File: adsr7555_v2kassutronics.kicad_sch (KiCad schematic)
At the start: 43 parts, among them J1 Power, J2 GateIn, J5 InvOut, J6 Output, Q1 3904, Q2 3904, Q3 3904, SW1 SW_Trig, U1 7555, U2 TL074

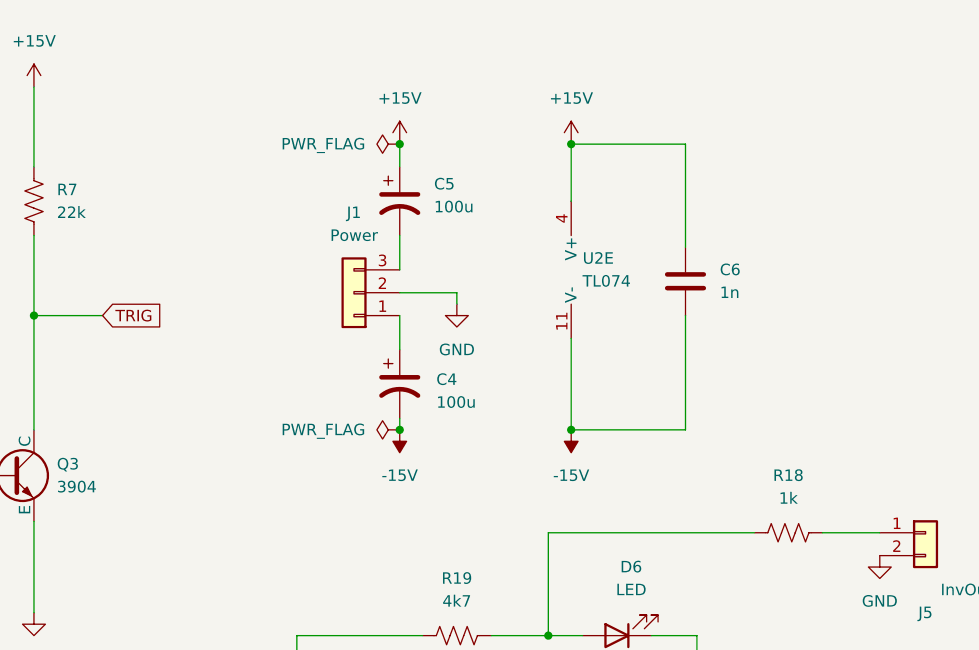
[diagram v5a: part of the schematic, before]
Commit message: cleaned up PCB wiring and designators
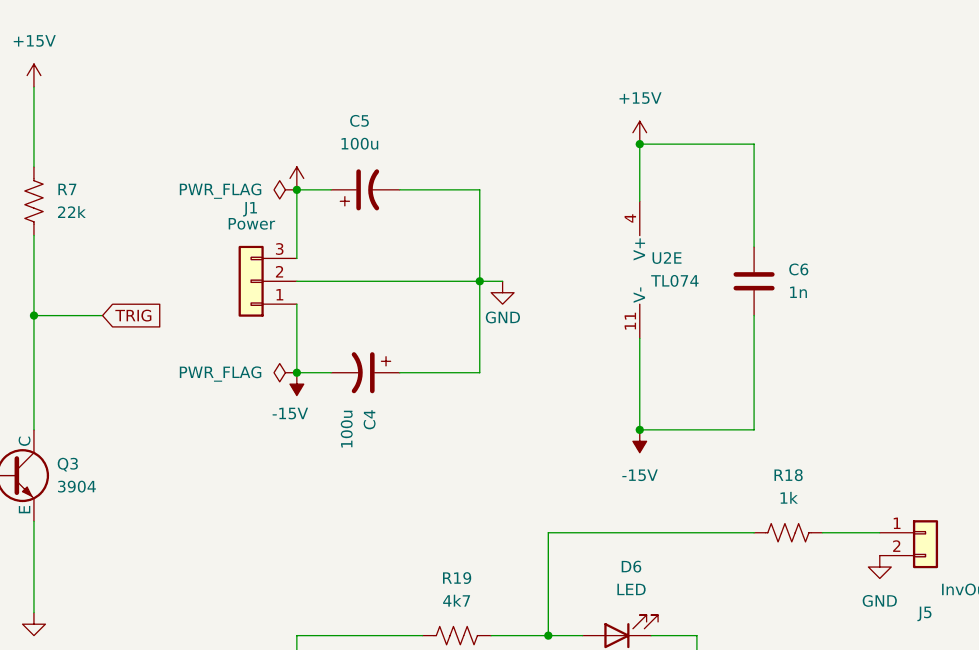
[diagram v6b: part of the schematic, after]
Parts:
- C4, C5: footprint Capacitor_THT:CP_Radial_D4.0mm_P2.00mm -> Capacitor_THT:CP_Radial_D5.0mm_P2.50mm
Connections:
- net +15V: now also J1.3 (Pin_3)
- net -15V: now also J1.1 (Pin_1)
- net GND: now also C4.1, C5.2
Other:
- moved on the sheet: C4, C5, C6, J1, U2E

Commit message: MAJOR FUP U2 was positioned backwards. Involved pt to pt silicon wires on bottom of PCB. Still not done
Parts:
- D4: footprint Diode_THT:D_DO-35_SOD27_P7.62mm_Horizontal -> Diode_THT:D_DO-35_SOD27_P2.54mm_Vertical_CathodeUp
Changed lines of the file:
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@@
 			)
 		)
-		(property "Footprint" "Diode_THT:D_DO-35_SOD27_P7.62mm_Horizontal"
+		(property "Footprint" "Diode_THT:D_DO-35_SOD27_P2.54mm_Vertical_CathodeUp"
 			(at 97.79 109.22 0)
 			(hide yes)
